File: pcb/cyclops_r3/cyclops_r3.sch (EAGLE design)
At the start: 78 parts, among them Q1 SUM11006, Q2 IRF510, U1 MCP4921, U2 TLV37, U3 317-N, U4 337-N, U5 ADR03, U6 OP1177, U7 LM324N, U8 ZXTD45

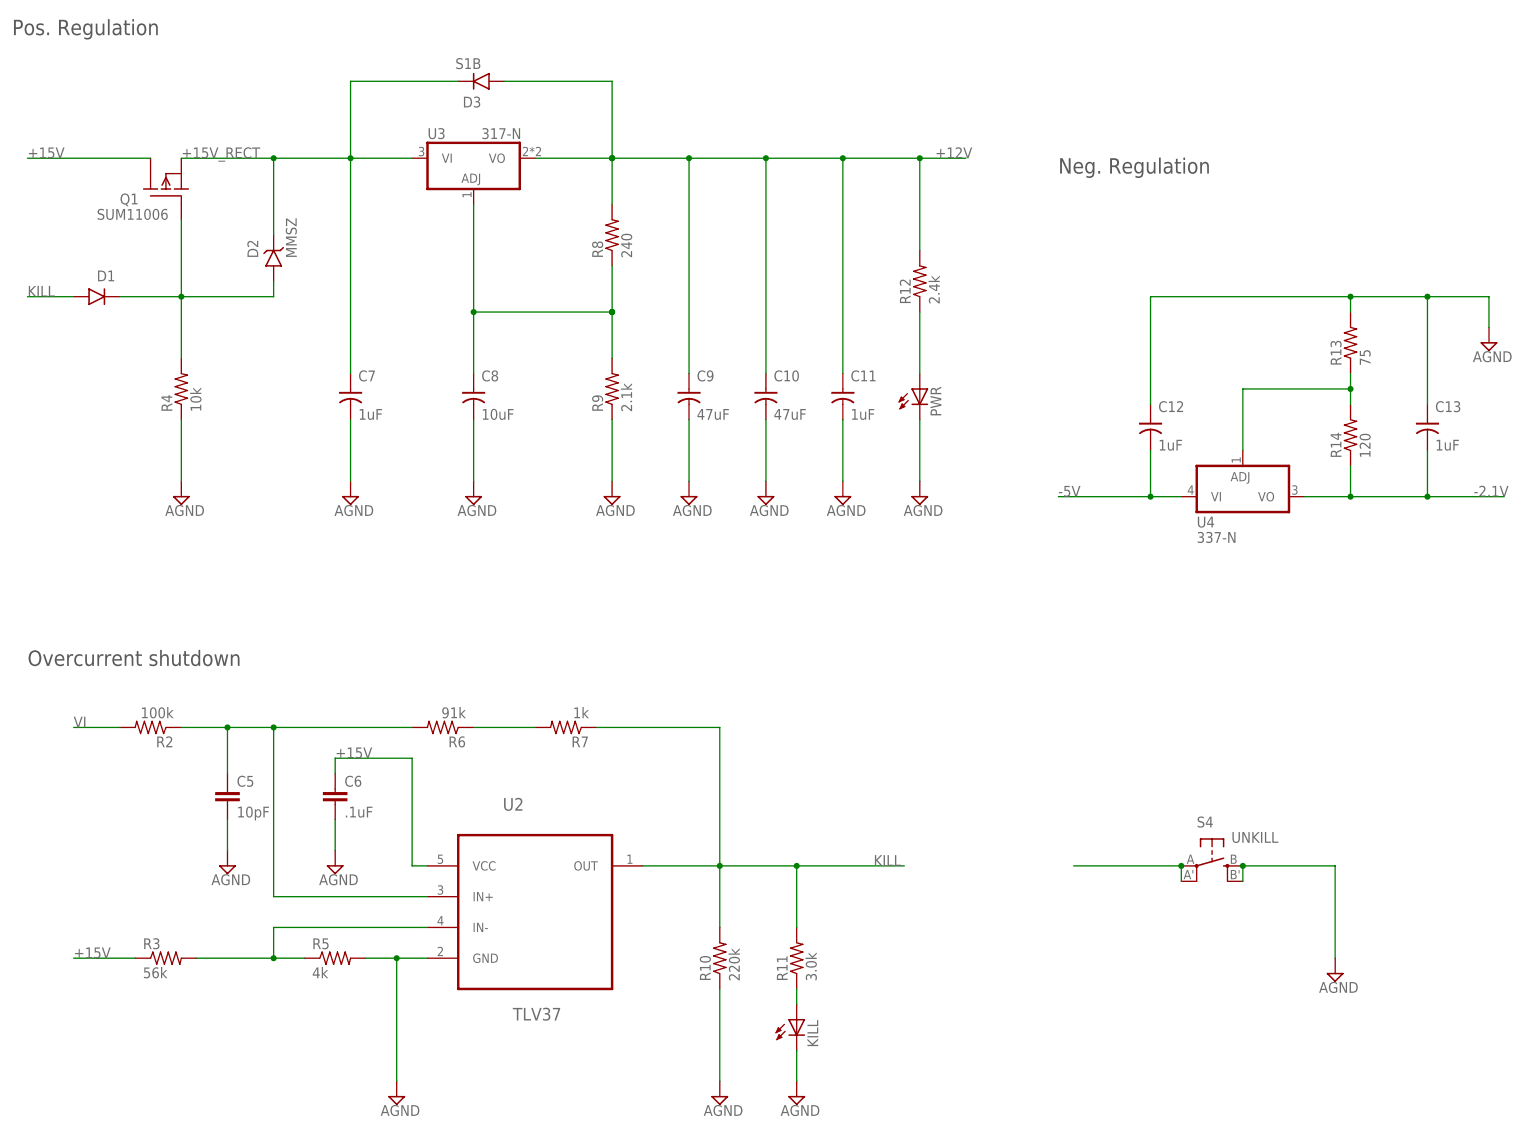
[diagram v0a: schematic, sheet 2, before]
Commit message: While breadboarding the overcurrent protection circuit, I found a problem with the PFET power switch. Documented in notes, but not fixed yet.
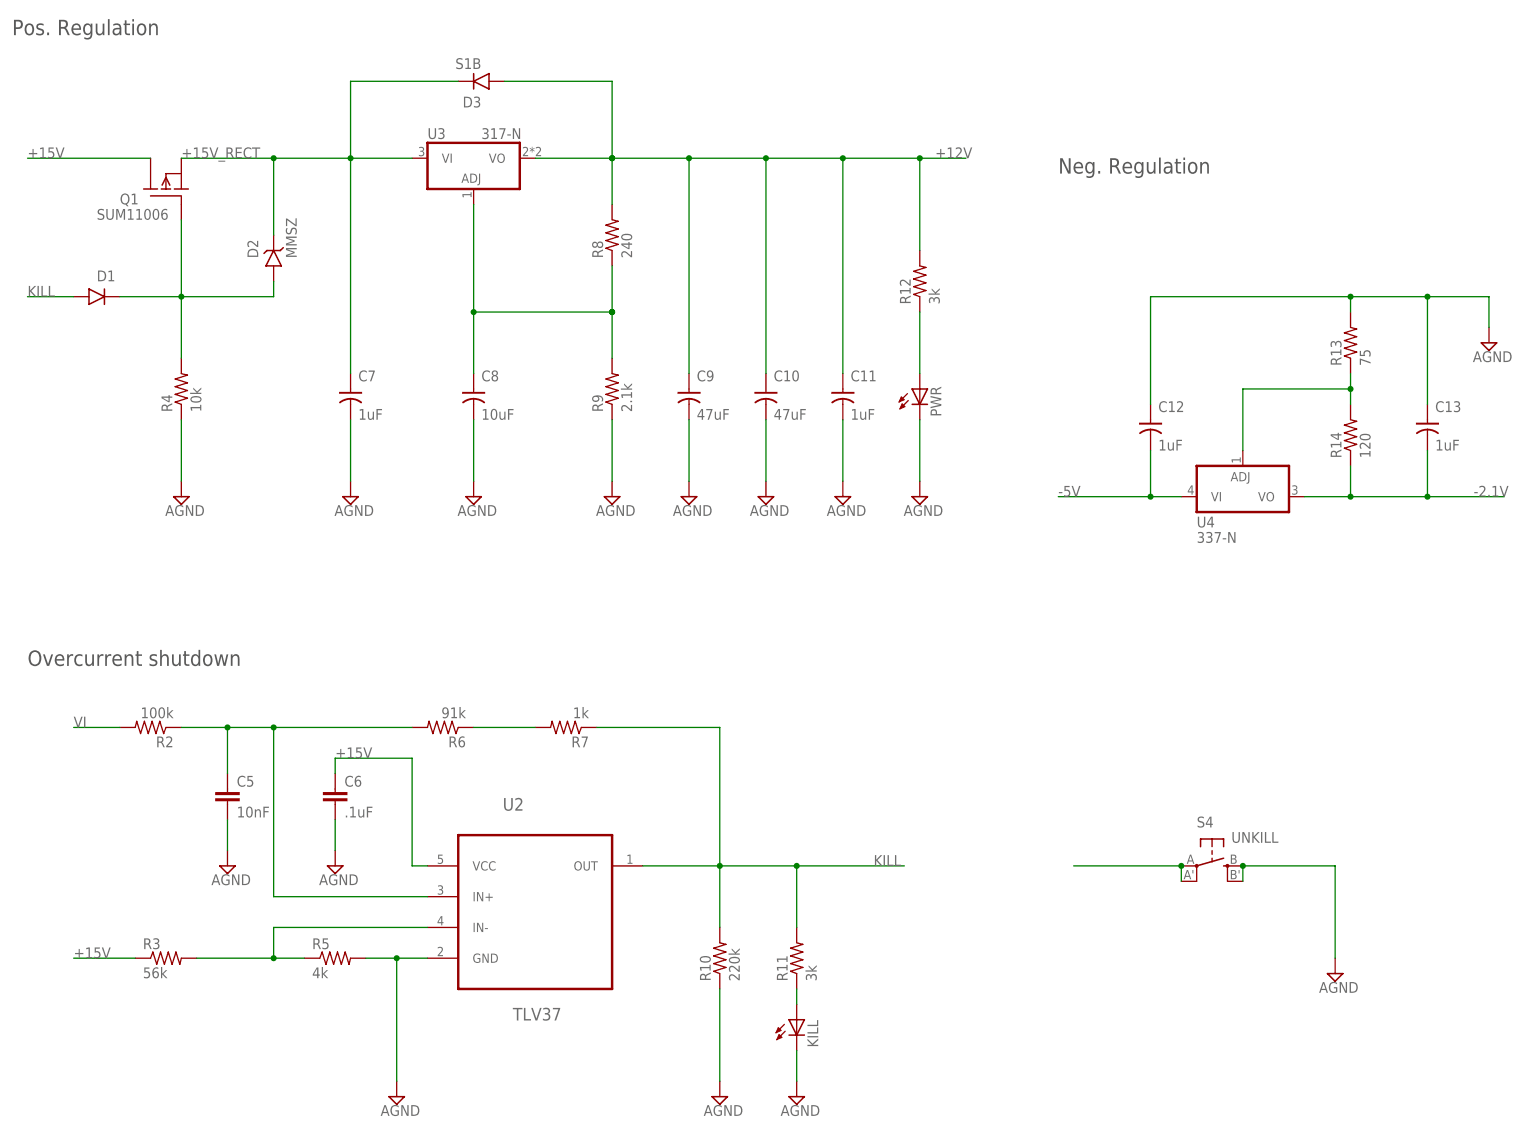
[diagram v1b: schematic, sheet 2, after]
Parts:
- C5: value 10pF -> 10nF
- R11: value 3.0k -> 3k
- R12: value 2.4k -> 3k
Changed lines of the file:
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@@
 <part name="VBIAS" library="cyclops" deviceset="TP" device="TP08R"/>
 <part name="VGATE" library="cyclops" deviceset="TP" device="TP08R"/>
-<part name="R12" library="cyclops" deviceset="R" device="_0603" value="2.4k"/>
+<part name="R12" library="cyclops" deviceset="R" device="_0603" value="3k"/>
 <part name="PWR" library="cyclops" deviceset="LED" device="_0805" technology="YELLOW"/>
 <part name="SUPPLY40" library="supply2" deviceset="AGND" device=""/>
@@
 <part name="C6" library="cyclops" deviceset="C" device="_0603" value=".1uF"/>
 <part name="SUPPLY43" library="cyclops" deviceset="AGND" device=""/>
-<part name="R11" library="cyclops" deviceset="R" device="_0603" value="3.0k"/>
+<part name="R11" library="cyclops" deviceset="R" device="_0603" value="3k"/>
 <part name="KILL" library="cyclops" deviceset="LED" device="_0805" technology="YELLOW"/>
 <part name="SUPPLY44" library="supply2" deviceset="AGND" device=""/>
-<part name="C5" library="cyclops" deviceset="C" device="_0603" value="10pF"/>
+<part name="C5" library="cyclops" deviceset="C" device="_0603" value="10nF"/>
 <part name="SUPPLY45" library="cyclops" deviceset="AGND" device=""/>
 <part name="S4" library="cyclops" deviceset="SPST_TACT" device="-EVQQ2" value="UNKILL"/>

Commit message: Fixing the overcurrent protection circuit.
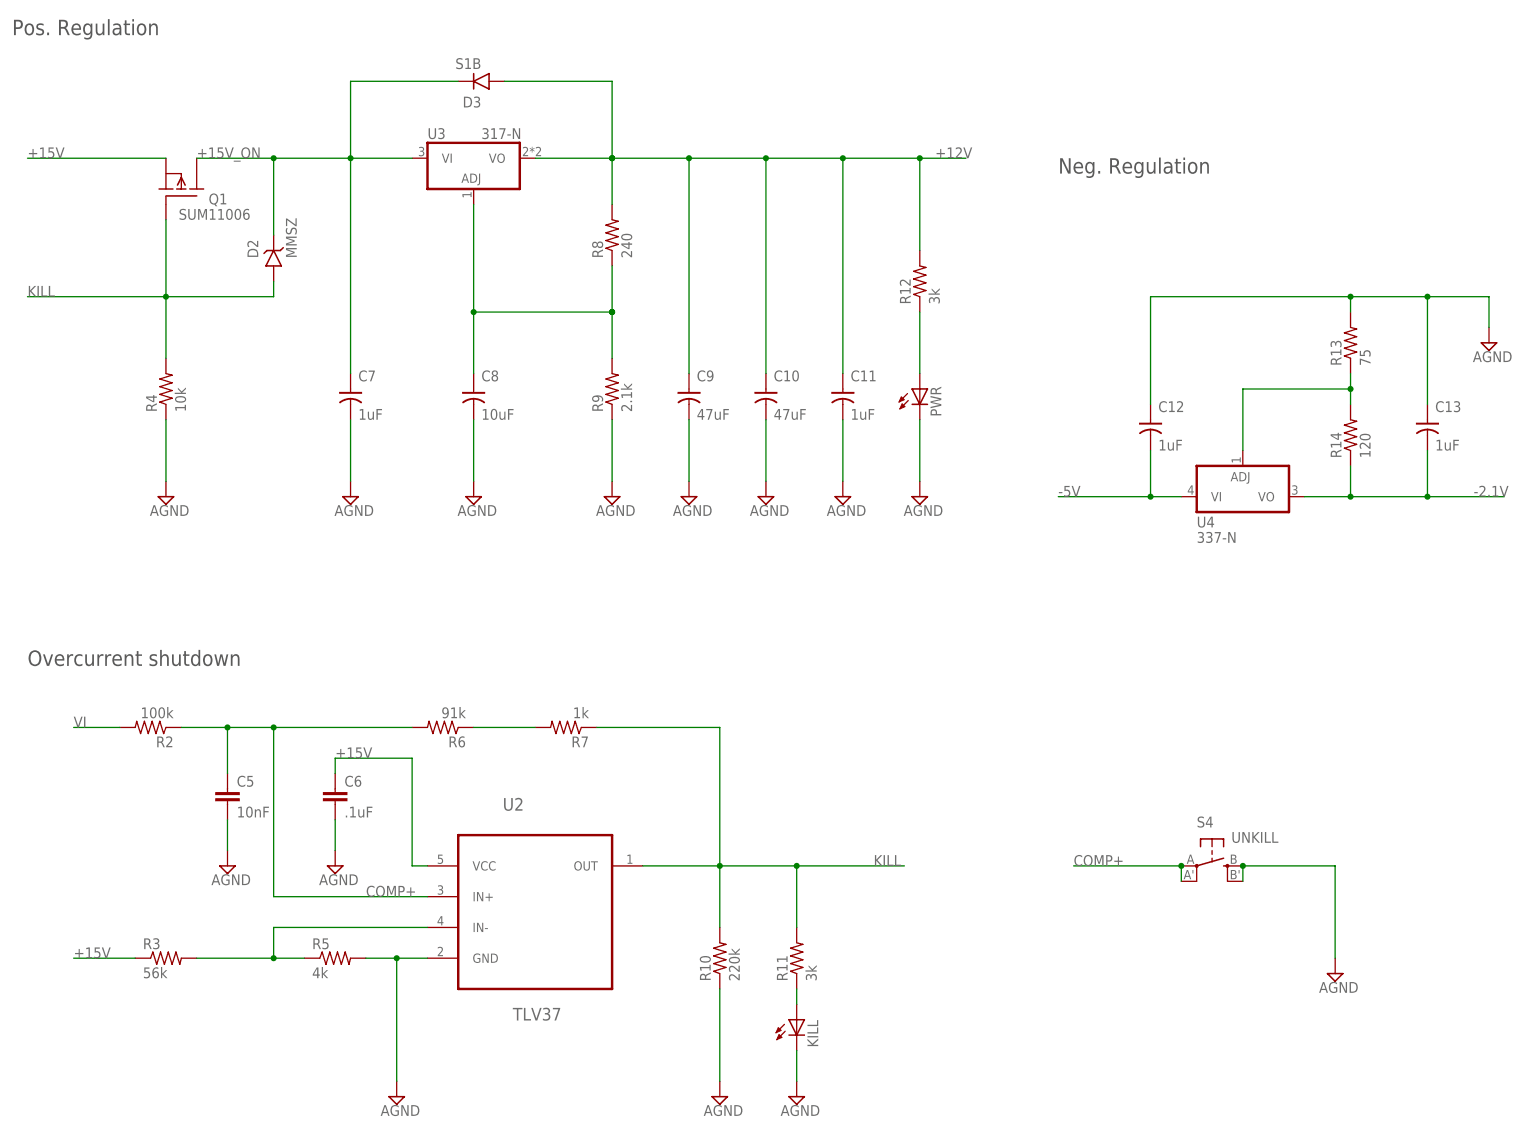
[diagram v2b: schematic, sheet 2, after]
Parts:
- removed D1: (no value), cyclops:DIODESOD-323
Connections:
- removed net +15V_RECT: C7.+, D2.C, D3.C, Q1.S, U3.VI
- removed net N$18: D1.C, D2.A, Q1.G, R4.2
- new net +15V_ON: C7.+, D2.C, D3.C, Q1.D, U3.VI
- net +15V: now also Q1.S; no longer Q1.D
- net KILL: now also D2.A, Q1.G, R4.2; no longer D1.A
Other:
- moved on the sheet: Q1, R4
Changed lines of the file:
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@@
 <part name="PWR" library="cyclops" deviceset="LED" device="_0805" technology="YELLOW"/>
 <part name="SUPPLY40" library="supply2" deviceset="AGND" device=""/>
-<part name="D1" library="cyclops" deviceset="DIODE" device="SOD-323"/>
 <part name="R10" library="cyclops" deviceset="R" device="_0603" value="220k"/>
 <part name="U2" library="ti-extended" deviceset="TLV3701CDBVT" device="" value="TLV37"/>
@@
 </segment>
 </net>
-<net name="+15V" class="1">
-<segment>
-<pinref part="I/O_BLOCK" gate="G$1" pin="1"/>
-<wire x1="43.18" y1="-5.08" x2="68.58" y2="-5.08" width="0.1524" layer="91"/>
-<label x="50.8" y="-5.08" size="1.778" layer="95"/>
-</segment>
-</net>
 <net name="LED-" class="0">
 <segment>
@@
 <wire x1="43.18" y1="-15.24" x2="68.58" y2="-15.24" width="0.1524" layer="91"/>
 <label x="50.8" y="-15.24" size="1.778" layer="95"/>
+</segment>
+</net>
+<net name="+15V" class="1">
+<segment>
+<pinref part="I/O_BLOCK" gate="G$1" pin="1"/>
+<wire x1="43.18" y1="-5.08" x2="68.58" y2="-5.08" width="0.1524" layer="91"/>
+<label x="50.8" y="-5.08" size="1.778" layer="95"/>
 </segment>
 </net>
@@
 <instance part="C10" gate="C" x="30.48" y="-5.08"/>
 <instance part="SUPPLY11" gate="G$1" x="-38.1" y="-20.32"/>
-<instance part="Q1" gate="G$1" x="-68.58" y="30.48" smashed="yes" rot="R90">
-<attribute name="VALUE" x="-80.01" y="25.4" size="1.778" layer="96"/>
-<attribute name="NAME" x="-76.2" y="27.94" size="1.778" layer="95"/>
-</instance>
-<instance part="R4" gate="R" x="-66.04" y="-2.54" smashed="yes" rot="R90">
-<attribute name="NAME" x="-67.5386" y="-6.35" size="1.778" layer="95" rot="R90"/>
-<attribute name="VALUE" x="-62.738" y="-6.35" size="1.778" layer="96" rot="R90"/>
-</instance>
-<instance part="SUPPLY20" gate="G$1" x="-66.04" y="-20.32"/>
+<instance part="Q1" gate="G$1" x="-66.04" y="30.48" smashed="yes" rot="MR90">
+<attribute name="VALUE" x="-54.61" y="25.4" size="1.778" layer="96" rot="MR0"/>
+<attribute name="NAME" x="-58.42" y="27.94" size="1.778" layer="95" rot="MR0"/>
+</instance>
+<instance part="R4" gate="R" x="-68.58" y="-2.54" smashed="yes" rot="R90">
+<attribute name="NAME" x="-70.0786" y="-6.35" size="1.778" layer="95" rot="R90"/>
+<attribute name="VALUE" x="-65.278" y="-6.35" size="1.778" layer="96" rot="R90"/>
+</instance>
+<instance part="SUPPLY20" gate="G$1" x="-68.58" y="-20.32"/>
 <instance part="D2" gate="G$1" x="-50.8" y="20.32" rot="R90"/>
 <instance part="FRAME2" gate="G$1" x="-109.22" y="-147.32"/>
@@
 <instance part="PWR" gate="G$1" x="55.88" y="-2.54"/>
 <instance part="SUPPLY40" gate="G$1" x="55.88" y="-20.32"/>
-<instance part="D1" gate="D" x="-81.28" y="12.7"/>
 <instance part="R10" gate="R" x="22.86" y="-96.52" smashed="yes" rot="R90">
 <attribute name="NAME" x="21.3614" y="-100.33" size="1.778" layer="95" rot="R90"/>
@@
 </busses>
 <nets>
-<net name="+15V" class="1">
-<segment>
+<net name="+15V_ON" class="1">
+<segment>
+<pinref part="U3" gate="A1" pin="VI"/>
+<wire x1="-38.1" y1="35.56" x2="-27.94" y2="35.56" width="0.1524" layer="91"/>
+<wire x1="-38.1" y1="35.56" x2="-38.1" y2="48.26" width="0.1524" layer="91"/>
+<pinref part="D3" gate="D" pin="C"/>
+<wire x1="-38.1" y1="48.26" x2="-20.32" y2="48.26" width="0.1524" layer="91"/>
+<junction x="-38.1" y="35.56"/>
+<pinref part="C7" gate="C" pin="+"/>
+<wire x1="-38.1" y1="0" x2="-38.1" y2="35.56" width="0.1524" layer="91"/>
+<label x="-63.5" y="35.56" size="1.778" layer="95"/>
+<pinref part="D2" gate="G$1" pin="C"/>
+<wire x1="-50.8" y1="35.56" x2="-38.1" y2="35.56" width="0.1524" layer="91"/>
+<wire x1="-50.8" y1="22.86" x2="-50.8" y2="35.56" width="0.1524" layer="91"/>
 <pinref part="Q1" gate="G$1" pin="D"/>
-<wire x1="-91.44" y1="35.56" x2="-71.12" y2="35.56" width="0.1524" layer="91"/>
-<label x="-91.44" y="35.56" size="1.778" layer="95"/>
-</segment>
-<segment>
-<pinref part="R3" gate="R" pin="1"/>
-<wire x1="-73.66" y1="-96.52" x2="-83.82" y2="-96.52" width="0.1524" layer="91"/>
-<label x="-83.82" y="-96.52" size="1.778" layer="95"/>
-</segment>
-<segment>
-<pinref part="U2" gate="A" pin="VCC"/>
-<wire x1="-25.4" y1="-81.28" x2="-27.94" y2="-81.28" width="0.1524" layer="91"/>
-<wire x1="-27.94" y1="-81.28" x2="-27.94" y2="-63.5" width="0.1524" layer="91"/>
-<pinref part="C6" gate="C" pin="1"/>
-<wire x1="-40.64" y1="-66.04" x2="-40.64" y2="-63.5" width="0.1524" layer="91"/>
-<wire x1="-40.64" y1="-63.5" x2="-27.94" y2="-63.5" width="0.1524" layer="91"/>
-<label x="-40.64" y="-63.5" size="1.778" layer="95"/>
+<wire x1="-50.8" y1="35.56" x2="-63.5" y2="35.56" width="0.1524" layer="91"/>
+<junction x="-50.8" y="35.56"/>
 </segment>
 </net>
@@
 <segment>
 <pinref part="R4" gate="R" pin="1"/>
-<wire x1="-66.04" y1="-7.62" x2="-66.04" y2="-17.78" width="0.1524" layer="91"/>
+<wire x1="-68.58" y1="-7.62" x2="-68.58" y2="-17.78" width="0.1524" layer="91"/>
 <pinref part="SUPPLY20" gate="G$1" pin="AGND"/>
 </segment>
@@
 <pinref part="SUPPLY47" gate="G$1" pin="AGND"/>
 <wire x1="149.86" y1="12.7" x2="149.86" y2="7.62" width="0.1524" layer="91"/>
-</segment>
-</net>
-<net name="N$18" class="0">
-<segment>
-<pinref part="Q1" gate="G$1" pin="G"/>
-<wire x1="-66.04" y1="2.54" x2="-66.04" y2="12.7" width="0.1524" layer="91"/>
-<pinref part="R4" gate="R" pin="2"/>
-<pinref part="D2" gate="G$1" pin="A"/>
-<wire x1="-66.04" y1="12.7" x2="-66.04" y2="25.4" width="0.1524" layer="91"/>
-<wire x1="-50.8" y1="15.24" x2="-50.8" y2="12.7" width="0.1524" layer="91"/>
-<wire x1="-50.8" y1="12.7" x2="-66.04" y2="12.7" width="0.1524" layer="91"/>
-<junction x="-66.04" y="12.7"/>
-<pinref part="D1" gate="D" pin="C"/>
-<wire x1="-76.2" y1="12.7" x2="-66.04" y2="12.7" width="0.1524" layer="91"/>
-</segment>
-</net>
-<net name="+15V_RECT" class="1">
-<segment>
-<pinref part="U3" gate="A1" pin="VI"/>
-<wire x1="-38.1" y1="35.56" x2="-27.94" y2="35.56" width="0.1524" layer="91"/>
-<wire x1="-38.1" y1="35.56" x2="-38.1" y2="48.26" width="0.1524" layer="91"/>
-<pinref part="D3" gate="D" pin="C"/>
-<wire x1="-38.1" y1="48.26" x2="-20.32" y2="48.26" width="0.1524" layer="91"/>
-<junction x="-38.1" y="35.56"/>
-<pinref part="C7" gate="C" pin="+"/>
-<wire x1="-38.1" y1="0" x2="-38.1" y2="35.56" width="0.1524" layer="91"/>
-<label x="-66.04" y="35.56" size="1.778" layer="95"/>
-<pinref part="Q1" gate="G$1" pin="S"/>
-<wire x1="-66.04" y1="35.56" x2="-50.8" y2="35.56" width="0.1524" layer="91"/>
-<pinref part="D2" gate="G$1" pin="C"/>
-<wire x1="-50.8" y1="35.56" x2="-38.1" y2="35.56" width="0.1524" layer="91"/>
-<wire x1="-50.8" y1="22.86" x2="-50.8" y2="35.56" width="0.1524" layer="91"/>
-<junction x="-50.8" y="35.56"/>
 </segment>
 </net>
@@
 </segment>
 <segment>
-<pinref part="D1" gate="D" pin="A"/>
-<wire x1="-91.44" y1="12.7" x2="-83.82" y2="12.7" width="0.1524" layer="91"/>
 <label x="-91.44" y="12.7" size="1.778" layer="95"/>
+<pinref part="Q1" gate="G$1" pin="G"/>
+<wire x1="-68.58" y1="2.54" x2="-68.58" y2="12.7" width="0.1524" layer="91"/>
+<pinref part="R4" gate="R" pin="2"/>
+<pinref part="D2" gate="G$1" pin="A"/>
+<wire x1="-68.58" y1="12.7" x2="-68.58" y2="25.4" width="0.1524" layer="91"/>
+<wire x1="-50.8" y1="15.24" x2="-50.8" y2="12.7" width="0.1524" layer="91"/>
+<wire x1="-50.8" y1="12.7" x2="-68.58" y2="12.7" width="0.1524" layer="91"/>
+<junction x="-68.58" y="12.7"/>
+<wire x1="-91.44" y1="12.7" x2="-68.58" y2="12.7" width="0.1524" layer="91"/>
 </segment>
 </net>
@@
 <wire x1="99.06" y1="-81.28" x2="99.06" y2="-83.82" width="0.1524" layer="91"/>
 <junction x="99.06" y="-81.28"/>
+<label x="81.28" y="-81.28" size="1.778" layer="95"/>
 </segment>
 <segment>
@@
 <wire x1="-58.42" y1="-66.04" x2="-58.42" y2="-58.42" width="0.1524" layer="91"/>
 <junction x="-58.42" y="-58.42"/>
+<label x="-35.56" y="-86.36" size="1.778" layer="95"/>
 </segment>
 </net>
@@
 </segment>
 </net>
+<net name="+15V" class="1">
+<segment>
+<pinref part="Q1" gate="G$1" pin="S"/>
+<wire x1="-68.58" y1="35.56" x2="-91.44" y2="35.56" width="0.1524" layer="91"/>
+<label x="-91.44" y="35.56" size="1.778" layer="95"/>
+</segment>
+<segment>
+<pinref part="R3" gate="R" pin="1"/>
+<wire x1="-73.66" y1="-96.52" x2="-83.82" y2="-96.52" width="0.1524" layer="91"/>
+<label x="-83.82" y="-96.52" size="1.778" layer="95"/>
+</segment>
+<segment>
+<pinref part="U2" gate="A" pin="VCC"/>
+<wire x1="-25.4" y1="-81.28" x2="-27.94" y2="-81.28" width="0.1524" layer="91"/>
+<wire x1="-27.94" y1="-81.28" x2="-27.94" y2="-63.5" width="0.1524" layer="91"/>
+<pinref part="C6" gate="C" pin="1"/>
+<wire x1="-40.64" y1="-66.04" x2="-40.64" y2="-63.5" width="0.1524" layer="91"/>
+<wire x1="-40.64" y1="-63.5" x2="-27.94" y2="-63.5" width="0.1524" layer="91"/>
+<label x="-40.64" y="-63.5" size="1.778" layer="95"/>
+</segment>
+</net>

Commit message: Almost finished with the layout. I need to fix the top silskcreen which provides pin information.
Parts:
- removed D5: DS11015, cyclops:S-DIODESOD-123
- added C22: .1uF, cyclops:C_0603
- added D1: MMSZ, cyclops:Z-DIODE_MMSZ
- C21: value .1uF -> ??
- D2: value MMSZ -> S1B; device cyclops:Z-DIODE_MMSZ -> cyclops:DIODES1B-13-F
- D3: value S1B -> DS11015; device cyclops:DIODES1B-13-F -> cyclops:S-DIODESOD-123
- KILL: value (none) -> LED; device cyclops:LEDYELLOW_0805 -> cyclops:LEDRED_0805
- PWR: value (none) -> LED; device cyclops:LEDYELLOW_0805 -> cyclops:LEDGREEN_0805
- R3: value 56k -> 10k
- R4: value 10k -> 56k
- U2: value TLV37 -> 317-N; device ti-extended:TLV3701CDBVT -> cyclops:317_TO263
- U3: value 317-N -> TLV37; device cyclops:317_TO263 -> ti-extended:TLV3701CDBVT
- U7: value LM324N -> TLV2374; device cyclops:LM324D -> cyclops:QUAD-OPAMP_14PIND
- VAUX: value (none) -> 361V509E
- renumbered U$1 to ARDUNIO
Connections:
- net +12V: now also C22.1, D2.A, D3.C, U2.VO; no longer C21.1, D3.A, D4.C, U3.VO
- net +15V: now also R4.1, U3.VCC; no longer R3.1, U2.VCC
- net +15V_ON: now also D1.C, U2.VI; no longer D3.C, U3.VI
- net COMP+: now also U3.IN+; no longer U2.IN+
- net GND: now also C22.2, D4.A, R3.1, U3.GND; no longer C21.2, D5.A, R4.1, U2.GND
- net KILL: now also D1.A, R3.2, U3.OUT; no longer D2.A, R4.2, U2.OUT
- net N$15: now also C21.2
- net N$5: now also R4.2, U3.IN-; no longer R3.2, U2.IN-
- net N$72: now also U2.ADJ; no longer U3.ADJ
- net VI: now also C21.1
- net _VREF: now also D3.A, D4.C; no longer D4.A, D5.C
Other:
- moved on the sheet: C21, D4, R21, R22, R3, R4
